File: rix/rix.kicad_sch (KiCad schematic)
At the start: 13 parts, among them J1 Barrel_Jack_Switch, J2 Conn_01x02_Male, J3 Conn_01x01_Male, U1 74LS04, U2 L78L05_SOT89, Y1 Crystal, Y2 Crystal

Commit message: PCB improvements
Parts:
- added D1: LED, Diode_SMD:D_1206_3216Metric_Pad1.42x1.75mm_HandSolder, symbol Device:LED
- added R3: 220R, Resistor_SMD:R_0805_2012Metric_Pad1.20x1.40mm_HandSolder, symbol Device:R
- C1: value C_Polarized -> 50v 10uF; footprint Capacitor_THT:CP_Radial_D8.0mm_P3.50mm -> Capacitor_THT:CP_Radial_D5.0mm_P2.00mm
- C2: value C_Polarized -> 50v 1uF; footprint Capacitor_THT:CP_Radial_D8.0mm_P3.80mm -> Capacitor_THT:CP_Radial_D5.0mm_P2.00mm
- C3: value C_Small -> 10nF; footprint Capacitor_SMD:C_1206_3216Metric_Pad1.33x1.80mm_HandSolder -> Capacitor_SMD:C_0805_2012Metric_Pad1.18x1.45mm_HandSolder
- J1: footprint Connector_BarrelJack:BarrelJack_Horizontal -> Connector_BarrelJack:BarrelJack_Kycon_KLDX-0202-xC_Horizontal
- J2: value Conn_01x02_Male -> Detection coil; footprint Connector_PinSocket_2.54mm:PinSocket_1x02_P2.54mm_Vertical -> Connector_PinHeader_2.54mm:PinHeader_1x02_P2.54mm_Vertical
- J3: value Conn_01x01_Male -> External antenna; footprint Connector_Pin:Pin_D1.4mm_L8.5mm_W2.8mm_FlatFork -> Connector_PinHeader_2.54mm:PinHeader_1x01_P2.54mm_Vertical
- R1: value R -> 1M
- RV1: value R_Potentiometer -> 10K
- U1: footprint Package_SO:SO-14_3.9x8.65mm_P1.27mm -> Package_SO:SOIC-14_3.9x8.7mm_P1.27mm
- Y1, Y2: value Crystal -> 8.0 Mhz Crystal
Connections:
- net GND: now also R3.1
- net at C2.1, C3.1, U1.14 (VCC)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: now also D1.1 (K)
- net IF: now reaches U1.4, U1.5
- net IF: now also U1.13; no longer Y2.2
- net at RV1.1, U1.6: now also Y1.2; no longer U1.9
- net at U1.10: now also R2.2, U1.9; no longer J3.1 (Pin_1)
- net at U1.8: now also J3.1 (Pin_1); no longer Y1.2
- new net: U1.12, Y2.1
- new net: D1.2 (A), R3.2
- new net: R2.1, U1.11, Y2.2
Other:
- note added: "Power supply"
- note added: "RF Amplifier"
- note added: "RIX Detector ALPHA"
- note added: "Ring-Xtal Oscillator"
- note added: "This metal detector combines a Ring OSC and a X-tal OSC into A BFO, the output (IF) of this BFO is then amplified and it's harmonics can be received in a common FM Radio receiver You can calculate IF's frecuency (in MHZ) using the next equation IF = Y1_Freq - 1/2N(T) where IF is the frequency in MHZ, Y1_1_Freq is the frequency of Xtal1, T is the average gate-delay time, and N is the number of gat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"
- note removed: "RIX Detector A"
- note removed: "v0.1.1 Alpha"
- title: (none) -> RIX Metal Detector by Dionys.
- moved on the sheet: C1, C2, C3, J1, J2, J3, R1, R2, RV1, U1A, U1B, U1C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

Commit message: Adding gerber files
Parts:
- removed RV1: 10K, Potentiometer_THT:Potentiometer_Alps_RK09K_Single_Vertical, symbol Device:R_Potentiometer
- added H1, H2, H3, H4: MountingHole_Pad, MountingHole:MountingHole_2.2mm_M2_DIN965_Pad_TopBottom, symbol Mechanical:MountingHole_Pad
- added RV1: 10K, Potentiometer_THT:Potentiometer_Alps_RK09K_Single_Vertical, symbol Device:R_Potentiometer_MountingPin
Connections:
- net GND: now also H1.1, H2.1, H3.1, H4.1, RV1.MP (MountPin)
- net at R1.2: now also RV1.1, RV1.2
- net at U1.6, Y1.2: now also RV1.3

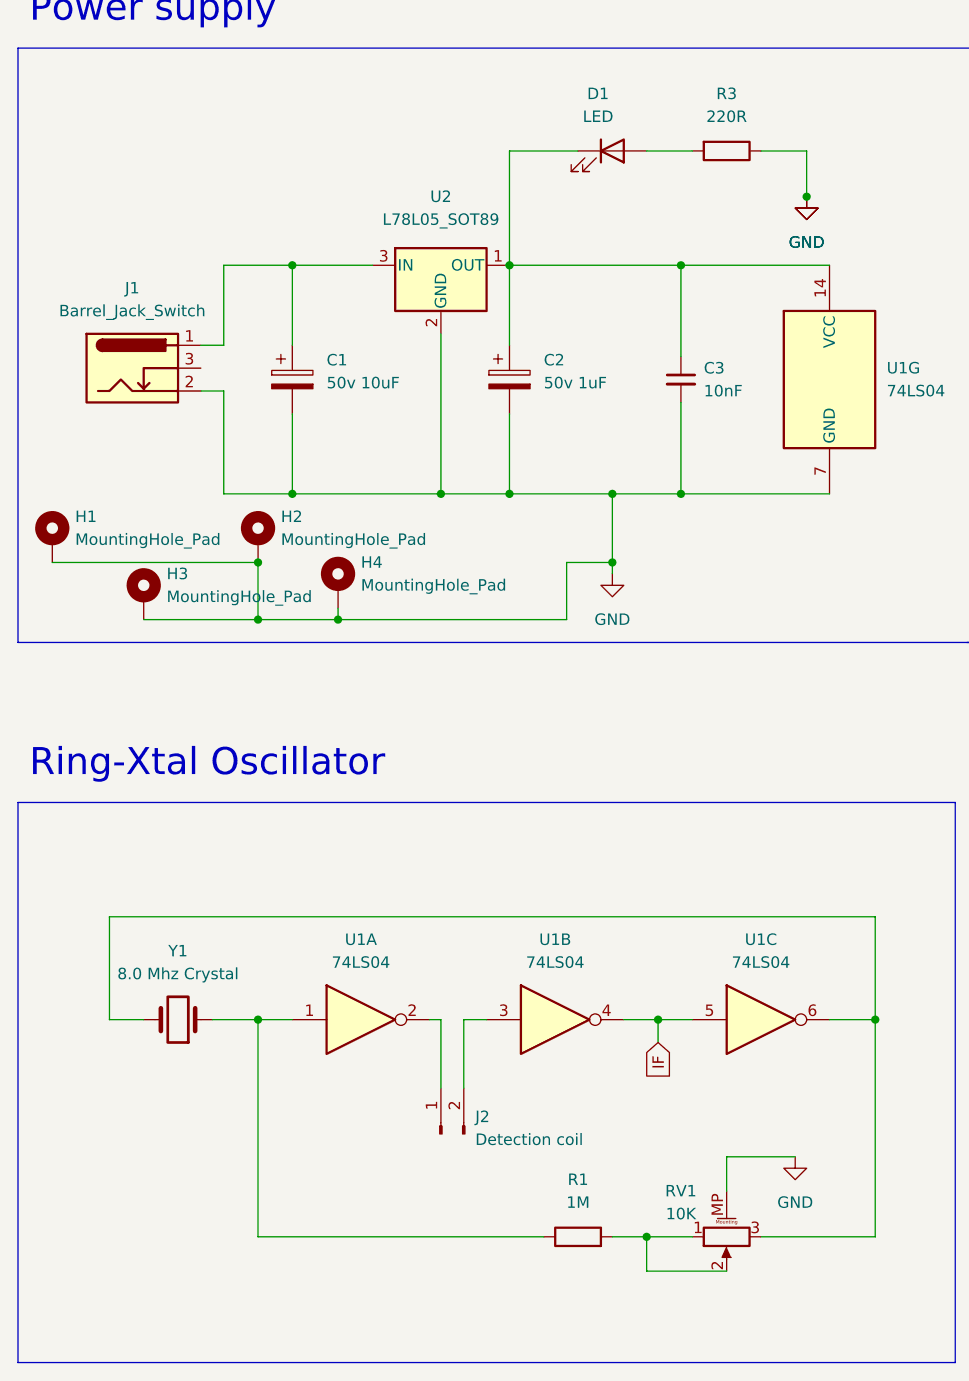
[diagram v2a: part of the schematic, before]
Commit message: Updating board constraits
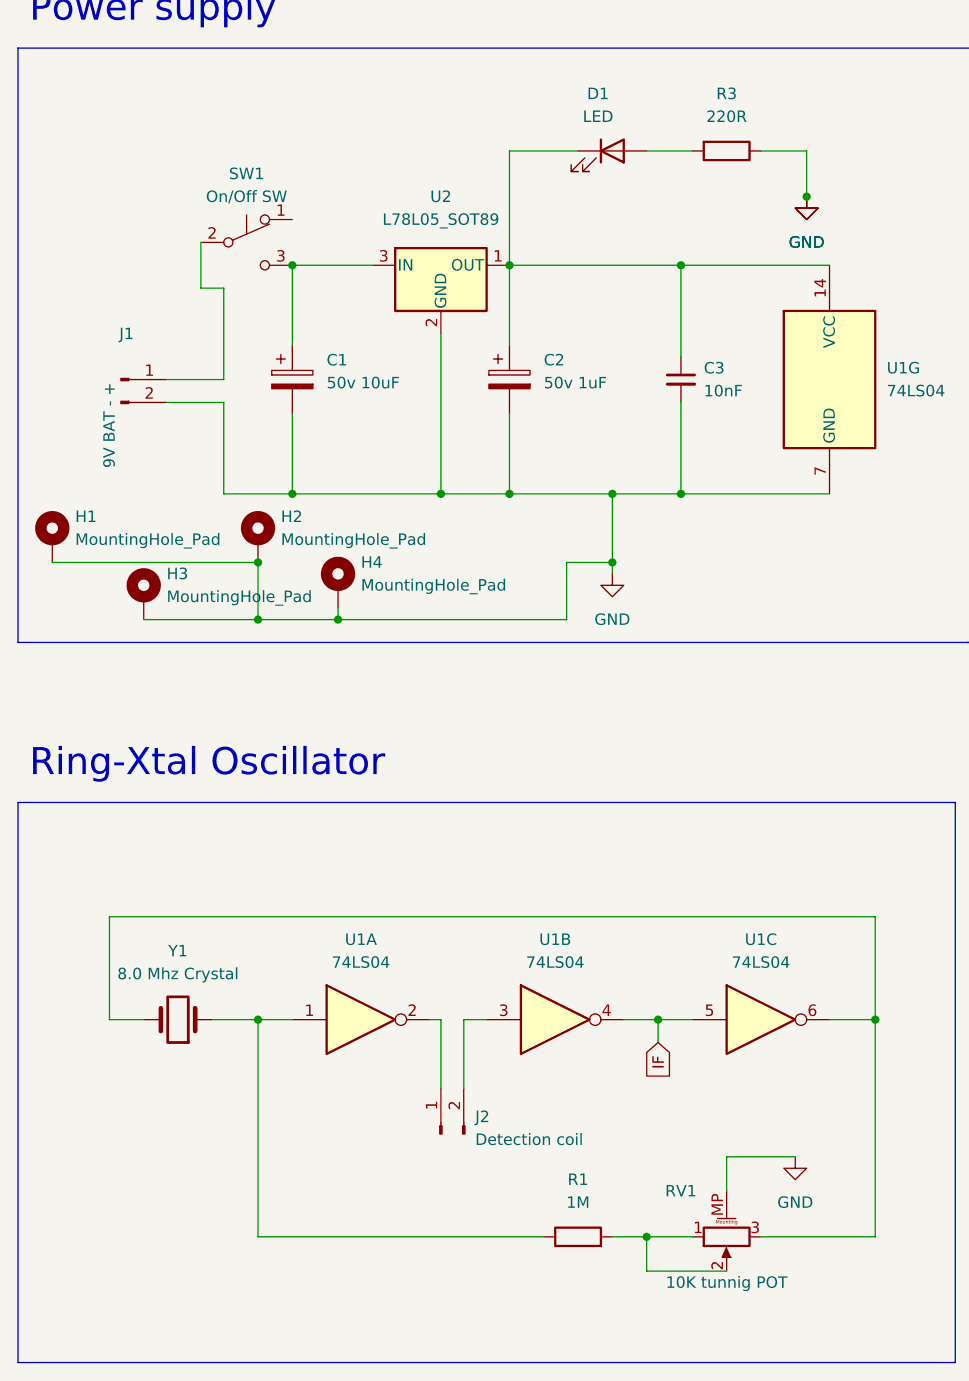
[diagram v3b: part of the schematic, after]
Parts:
- removed J1: Barrel_Jack_Switch, Connector_BarrelJack:BarrelJack_Kycon_KLDX-0202-xC_Horizontal, symbol Connector:Barrel_Jack_Switch
- added J1: 9V BAT - +, Connector_JST:JST_PH_B2B-PH-K_1x02_P2.00mm_Vertical, symbol Connector:Conn_01x02_Male
- added SW1: On/Off SW, Button_Switch_THT:SW_Push_1P2T_Vertical_E-Switch_800UDP8P1A1M6, symbol Switch:SW_Push_SPDT
- RV1: value 10K -> 10K tunnig POT
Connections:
- net GND: now also J1.2 (Pin_2)
- net at C1.1, U2.3 (IN): now also SW1.3 (C)
- new net: J1.1 (Pin_1), SW1.2 (B)

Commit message: Updating gerber files
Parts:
- removed J1: 9V BAT - +, Connector_JST:JST_PH_B2B-PH-K_1x02_P2.00mm_Vertical, symbol Connector:Conn_01x02_Male
- removed J2: Detection coil, Connector_PinHeader_2.54mm:PinHeader_1x02_P2.54mm_Vertical, symbol Connector:Conn_01x02_Male
- removed J3: External antenna, Connector_PinHeader_2.54mm:PinHeader_1x01_P2.54mm_Vertical, symbol Connector:Conn_01x01_Male
- removed RV1: 10K tunnig POT, Potentiometer_THT:Potentiometer_Alps_RK09K_Single_Vertical, symbol Device:R_Potentiometer_MountingPin
- removed SW1: On/Off SW, Button_Switch_THT:SW_Push_1P2T_Vertical_E-Switch_800UDP8P1A1M6, symbol Switch:SW_Push_SPDT
- removed U1: 74LS04, Package_SO:SOIC-14_3.9x8.7mm_P1.27mm, symbol 74xx:74LS04
- removed U2: L78L05_SOT89, Package_TO_SOT_SMD:SOT-89-3, symbol Regulator_Linear:L78L05_SOT89
- removed Y2: 8.0 Mhz Crystal, Crystal:Crystal_HC49-4H_Vertical, symbol Device:Crystal
- added C4: C_Small, Capacitor_THT:C_Disc_D3.8mm_W2.6mm_P2.50mm, symbol Device:C_Small
- added D2, D3, D4, D5, D6, D7, D8: LED, LED_THT:LED_D3.0mm, symbol Device:LED
- added H5: MountingHole_Pad, MountingHole:MountingHole_2.2mm_M2_DIN965_Pad_TopBottom, symbol Mechanical:MountingHole_Pad
- added J1, J2: AudioJack3_SwitchTR, Connector_Audio:Jack_3.5mm_Ledino_KB3SPRS_Horizontal, symbol Connector:AudioJack3_SwitchTR
- added J3: Conn_01x02_Male, Connector_JST:JST_XH_B2B-XH-A_1x02_P2.50mm_Vertical, symbol Connector:Conn_01x02_Male
- added J4: Barrel_Jack_Switch, Connector_BarrelJack:BarrelJack_Horizontal, symbol Connector:Barrel_Jack_Switch
- added Q1: IRFS4127, Package_TO_SOT_THT:TO-92_Wide, symbol Transistor_FET:IRFS4127
- added R10, R11, R12, R13, R4, R5, R6, R7, R8, R9: R, Resistor_THT:R_Axial_DIN0204_L3.6mm_D1.6mm_P5.08mm_Horizontal, symbol Device:R
- added SW1: SW_DIP_x01, Button_Switch_THT:SW_PUSH_6mm_H5mm, symbol Switch:SW_DIP_x01
- added SW2: SW_Push_DPDT, Button_Switch_THT:SW_Push_2P2T_Toggle_CK_PVA2OAH5xxxxxxV2, symbol Switch:SW_Push_DPDT
- added U1: 74LS02, Package_DIP:DIP-14_W7.62mm, symbol 74xx:74LS02
- added U2: L78L05_TO92, Package_TO_SOT_THT:TO-92_Wide, symbol Regulator_Linear:L78L05_TO92
- added U3: TL431PK, Package_TO_SOT_THT:TO-92_Wide, symbol Reference_Voltage:TL431PK
- C1: value 50v 10uF -> C_Polarized; footprint Capacitor_THT:CP_Radial_D5.0mm_P2.00mm -> Capacitor_THT:CP_Radial_D6.3mm_P2.50mm
- C2: value 50v 1uF -> C_Polarized; footprint Capacitor_THT:CP_Radial_D5.0mm_P2.00mm -> Capacitor_THT:CP_Radial_D6.3mm_P2.50mm
- C3: value 10nF -> C_Small; footprint Capacitor_SMD:C_0805_2012Metric_Pad1.18x1.45mm_HandSolder -> Capacitor_THT:C_Disc_D3.8mm_W2.6mm_P2.50mm
- D1: footprint Diode_SMD:D_1206_3216Metric_Pad1.42x1.75mm_HandSolder -> LED_THT:LED_D3.0mm
- R1: value 1M -> R; footprint Resistor_SMD:R_0805_2012Metric_Pad1.20x1.40mm_HandSolder -> Resistor_THT:R_Axial_DIN0204_L3.6mm_D1.6mm_P5.08mm_Horizontal
- R2: value 1K -> R; footprint Resistor_SMD:R_0805_2012Metric_Pad1.20x1.40mm_HandSolder -> Resistor_THT:R_Axial_DIN0204_L3.6mm_D1.6mm_P5.08mm_Horizontal
- R3: value 220R -> R; footprint Resistor_SMD:R_0805_2012Metric_Pad1.20x1.40mm_HandSolder -> Resistor_THT:R_Axial_DIN0204_L3.6mm_D1.6mm_P5.08mm_Horizontal
- Y1: value 8.0 Mhz Crystal -> Crystal
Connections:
- net GND: now also D1.1 (K), C4.2, H5.1, SW2.6 (C), U1.7 (GND), U2.2 (GND); no longer R3.1
- net +9V: now reaches C1.1
- net +9V: now also R1.1, J3.2 (Pin_2), J4.1, SW1.2, SW2.2 (B), U2.3 (VI)
- net at R3.2: now also D2.1 (K); no longer D1.2 (A)
- net at C2.1, C3.1: now also C4.1, U1.14 (VCC), U2.1 (VO); no longer D1.1 (K)
- net at Y1.1: now also U1.13; no longer R1.1
- net at R1.2: now also D1.2 (A)
- net at R2.1: now also U1.1, U1.5, U1.6
- net at R2.2: now also Y1.2, U1.2, U1.3
- new net: J3.1 (Pin_1), R3.1, R4.1, R5.1, R6.1, R7.1, SW2.5 (B)
- new net: D2.2 (A), D3.1 (K), R4.2
- new net: J1.R, J1.RN, J1.S, J1.TN, U1.4
- new net: J1.T, U1.8, U1.9
- new net: J4.2, Q1.3 (S), R13.2, R8.2, U3.2 (A)
- new net: D7.1 (K), D8.2 (A), Q1.1 (G), R11.2, U3.3 (K)
- new net: Q1.2 (D), SW2.4 (A)
- new net: D4.2 (A), D5.1 (K), R6.2
- new net: D8.1 (K), R13.1
- new net: D6.2 (A), R10.1, R11.1, R12.1, SW1.1, SW2.1 (A)
- new net: D7.2 (A), R12.2
- new net: R8.1, R9.2
- new net: R10.2, R9.1, U3.1 (REF)
- new net: D5.2 (A), D6.1 (K), R7.2
- new net: J2.T, U1.11, U1.12
- new net: J2.R, J2.RN, J2.S, J2.TN, U1.10
- new net: D3.2 (A), D4.1 (K), R5.2
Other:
- note added: "This metal detector combines a Ring OSC and a X-tal OSC, the output of this OSC is then amplified and it's harmonics can be received in a common FM Radio receiver Use SW1 to check battery level, SW2 to turn ON/OFF the device, Connect your search coils to J1 and J2. Connect a 9v baterry to j3, connect a 12V power source to J4 to charge the device."
- note removed: "Power supply"
- note removed: "RF Amplifier"
- note removed: "Ring-Xtal Oscillator"
- note removed: "This metal detector combines a Ring OSC and a X-tal OSC into A BFO, the output (IF) of this BFO is then amplified and it's harmonics can be received in a common FM Radio receiver You can calculate IF's frecuency (in MHZ) using the next equation IF = Y1_Freq - 1/2N(T) where IF is the frequency in MHZ, Y1_1_Freq is the frequency of Xtal1, T is the average gate-delay time, and N is the number of gat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"

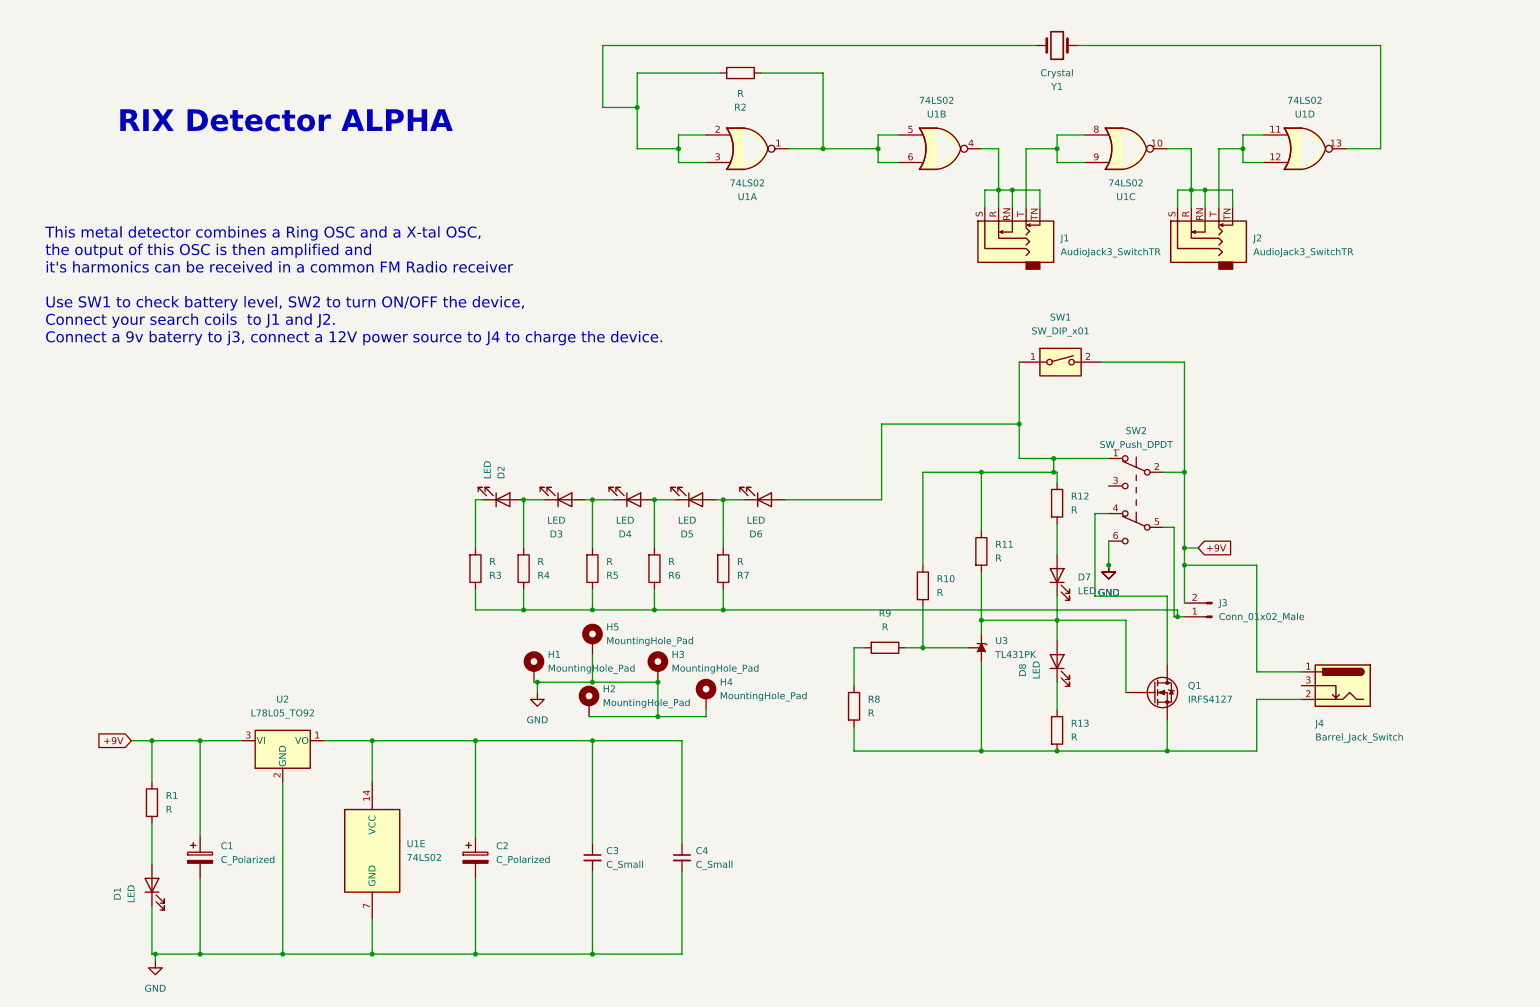
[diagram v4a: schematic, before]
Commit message: Uptating req Kicad7
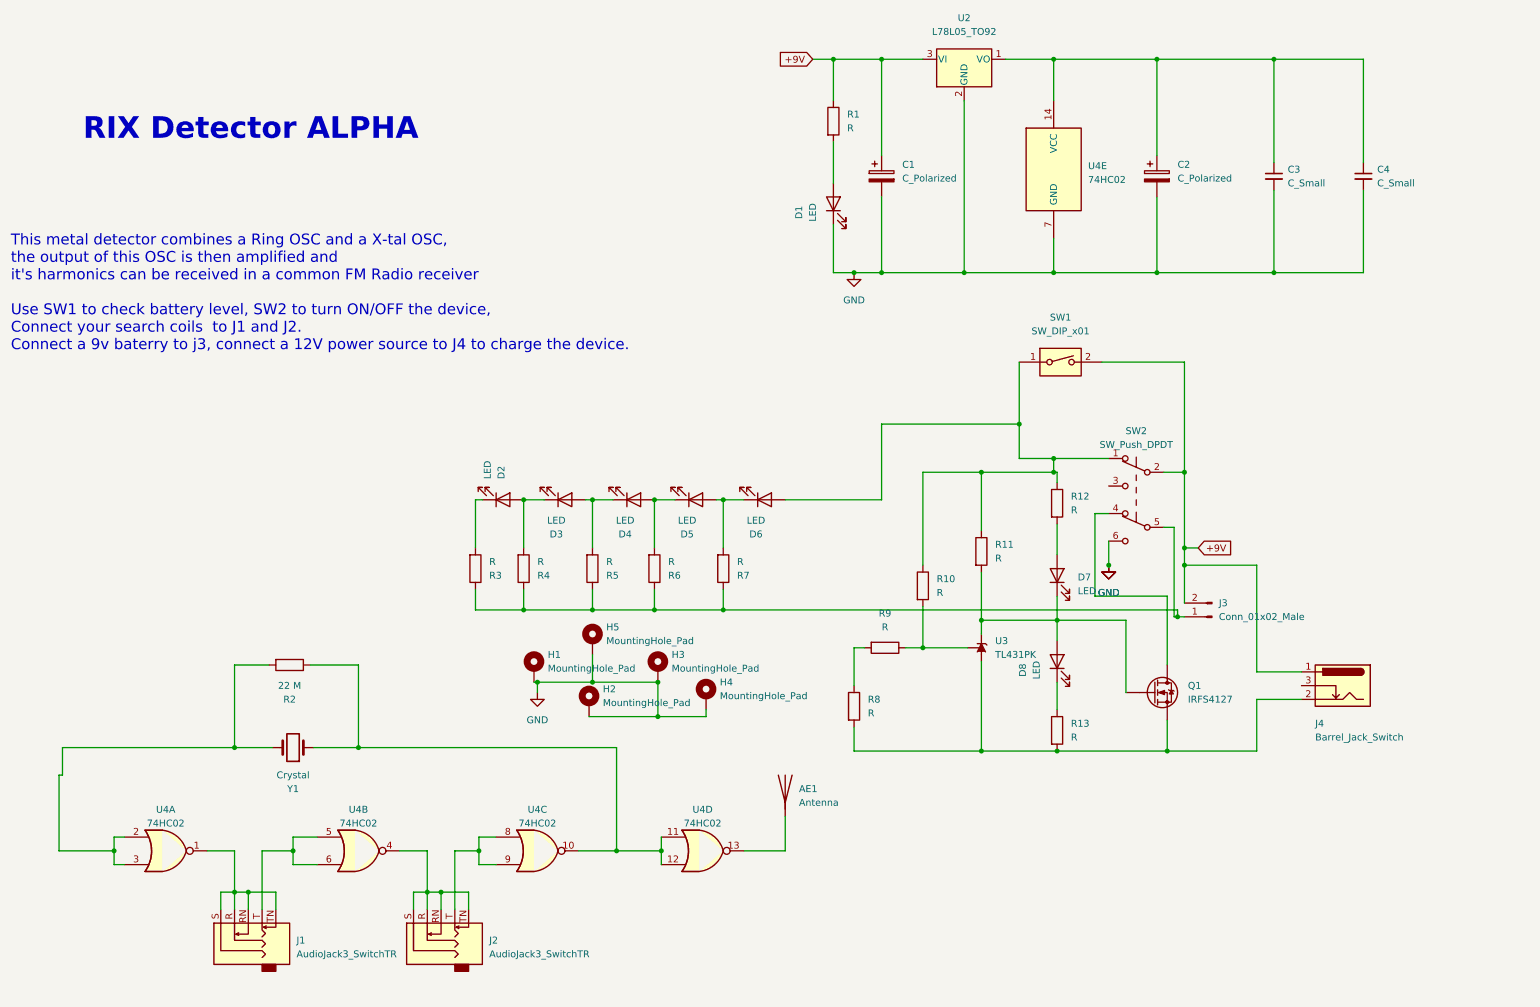
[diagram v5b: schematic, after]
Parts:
- removed U1: 74LS02, Package_DIP:DIP-14_W7.62mm, symbol 74xx:74LS02
- added AE1: Antenna, Connector_PinHeader_1.00mm:PinHeader_1x01_P1.00mm_Vertical, symbol Device:Antenna
- added U4: 74HC02, Package_DIP:DIP-14_W7.62mm, symbol 74xx:74HC02
- R2: value R -> 22 M
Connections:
- net GND: now also U4.7 (GND)
- net at C2.1, C3.1, C4.1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: now also U4.14 (VCC)
- net at J1.R, J1.RN, J1.S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: now also U4.1
- net at J1.T: now also U4.5, U4.6
- net at R2.1: now also Y1.1, U4.10, U4.11, U4.12
- net at J2.T: now also U4.8, U4.9
- net at J2.R, J2.RN, J2.S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: now also U4.4
- net at R2.2, Y1.2: now also U4.2, U4.3
- new net: AE1.1 (A), U4.13
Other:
- moved on the sheet: C1, C2, C3, C4, D1, J1, J2, R1, R2, U2, Y1
